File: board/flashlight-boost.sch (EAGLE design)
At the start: 9 parts

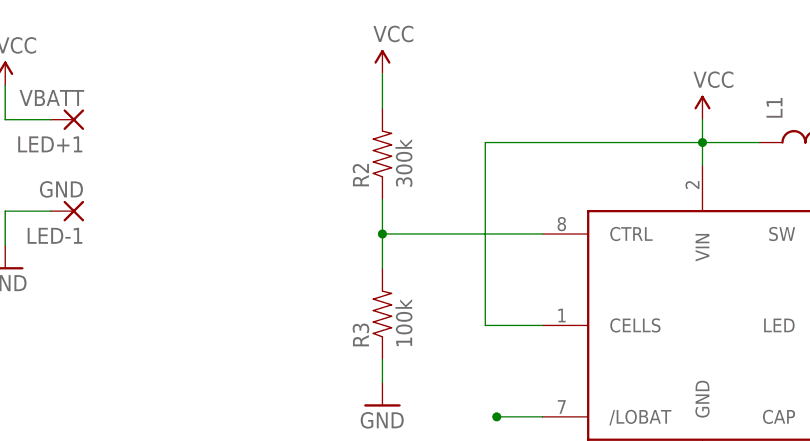
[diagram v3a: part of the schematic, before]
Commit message: Fixing voltage divider.
The voltage divider was setup to yield a control voltage of 0.6v which for a 2.4v input sets up the LED driver for a driver current of just over 25mA.  The drive current should be between 80mA and 100mA.  Lowering R1 in the divider to somewhere between 178k and 150k will do just that.
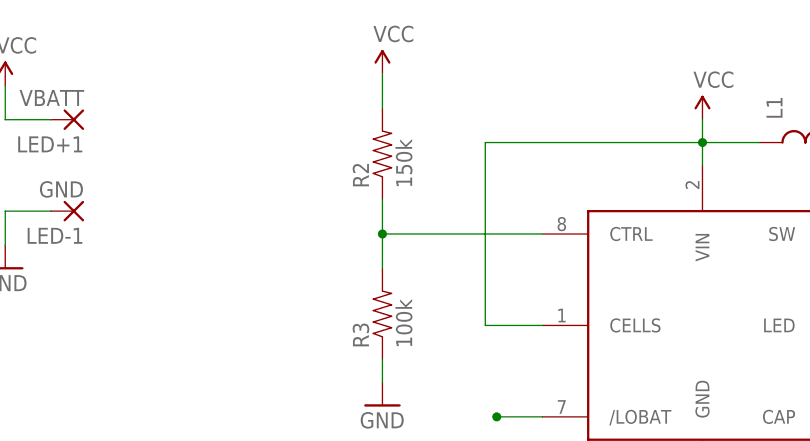
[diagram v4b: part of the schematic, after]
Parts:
- R2: value 300k -> 150k
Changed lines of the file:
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@@
 <setting verticaltext="up"/>
 </settings>
-<grid distance="0.05" unitdist="inch" unit="inch" style="lines" multiple="1" display="yes" altdistance="0.005" altunitdist="inch" altunit="inch"/>
+<grid distance="0.1" unitdist="inch" unit="inch" style="lines" multiple="1" display="no" altdistance="0.01" altunitdist="inch" altunit="inch"/>
 <layers>
-<layer number="1" name="Top" color="4" fill="1" visible="yes" active="no"/>
-<layer number="16" name="Bottom" color="1" fill="1" visible="yes" active="no"/>
-<layer number="17" name="Pads" color="2" fill="1" visible="yes" active="no"/>
-<layer number="18" name="Vias" color="2" fill="1" visible="yes" active="no"/>
-<layer number="19" name="Unrouted" color="6" fill="1" visible="yes" active="no"/>
-<layer number="20" name="Dimension" color="15" fill="1" visible="yes" active="no"/>
-<layer number="21" name="tPlace" color="16" fill="1" visible="yes" active="no"/>
-<layer number="22" name="bPlace" color="14" fill="1" visible="yes" active="no"/>
-<layer number="23" name="tOrigins" color="15" fill="1" visible="yes" active="no"/>
-<layer number="24" name="bOrigins" color="15" fill="1" visible="yes" active="no"/>
-<layer number="25" name="tNames" color="7" fill="1" visible="yes" active="no"/>
-<layer number="26" name="bNames" color="7" fill="1" visible="yes" active="no"/>
-<layer number="27" name="tValues" color="7" fill="1" visible="yes" active="no"/>
-<layer number="28" name="bValues" color="7" fill="1" visible="yes" active="no"/>
+<layer number="1" name="Top" color="4" fill="1" visible="no" active="no"/>
+<layer number="16" name="Bottom" color="1" fill="1" visible="no" active="no"/>
+<layer number="17" name="Pads" color="2" fill="1" visible="no" active="no"/>
+<layer number="18" name="Vias" color="2" fill="1" visible="no" active="no"/>
+<layer number="19" name="Unrouted" color="6" fill="1" visible="no" active="no"/>
+<layer number="20" name="Dimension" color="15" fill="1" visible="no" active="no"/>
+<layer number="21" name="tPlace" color="16" fill="1" visible="no" active="no"/>
+<layer number="22" name="bPlace" color="14" fill="1" visible="no" active="no"/>
+<layer number="23" name="tOrigins" color="15" fill="1" visible="no" active="no"/>
+<layer number="24" name="bOrigins" color="15" fill="1" visible="no" active="no"/>
+<layer number="25" name="tNames" color="7" fill="1" visible="no" active="no"/>
+<layer number="26" name="bNames" color="7" fill="1" visible="no" active="no"/>
+<layer number="27" name="tValues" color="7" fill="1" visible="no" active="no"/>
+<layer number="28" name="bValues" color="7" fill="1" visible="no" active="no"/>
 <layer number="29" name="tStop" color="7" fill="3" visible="no" active="no"/>
 <layer number="30" name="bStop" color="7" fill="6" visible="no" active="no"/>
@@
 <layer number="35" name="tGlue" color="7" fill="4" visible="no" active="no"/>
 <layer number="36" name="bGlue" color="7" fill="5" visible="no" active="no"/>
-<layer number="37" name="tTest" color="7" fill="1" visible="yes" active="no"/>
-<layer number="38" name="bTest" color="7" fill="1" visible="yes" active="no"/>
+<layer number="37" name="tTest" color="7" fill="1" visible="no" active="no"/>
+<layer number="38" name="bTest" color="7" fill="1" visible="no" active="no"/>
 <layer number="39" name="tKeepout" color="4" fill="11" visible="no" active="no"/>
 <layer number="40" name="bKeepout" color="1" fill="11" visible="no" active="no"/>
@@
 <layer number="44" name="Drills" color="7" fill="1" visible="no" active="no"/>
 <layer number="45" name="Holes" color="7" fill="1" visible="no" active="no"/>
-<layer number="46" name="Milling" color="3" fill="1" visible="yes" active="no"/>
-<layer number="47" name="Measures" color="7" fill="1" visible="yes" active="no"/>
-<layer number="48" name="Document" color="7" fill="1" visible="yes" active="no"/>
-<layer number="49" name="Reference" color="7" fill="1" visible="yes" active="no"/>
-<layer number="50" name="dxf" color="7" fill="1" visible="yes" active="no"/>
-<layer number="51" name="tDocu" color="6" fill="1" visible="yes" active="no"/>
-<layer number="52" name="bDocu" color="7" fill="1" visible="yes" active="no"/>
-<layer number="53" name="tGND_GNDA" color="7" fill="9" visible="yes" active="no"/>
-<layer number="54" name="bGND_GNDA" color="1" fill="9" visible="yes" active="no"/>
-<layer number="56" name="wert" color="7" fill="1" visible="yes" active="no"/>
+<layer number="46" name="Milling" color="3" fill="1" visible="no" active="no"/>
+<layer number="47" name="Measures" color="7" fill="1" visible="no" active="no"/>
+<layer number="48" name="Document" color="7" fill="1" visible="no" active="no"/>
+<layer number="49" name="Reference" color="7" fill="1" visible="no" active="no"/>
+<layer number="50" name="dxf" color="7" fill="1" visible="no" active="no"/>
+<layer number="51" name="tDocu" color="6" fill="1" visible="no" active="no"/>
+<layer number="52" name="bDocu" color="7" fill="1" visible="no" active="no"/>
+<layer number="53" name="tGND_GNDA" color="7" fill="9" visible="no" active="no"/>
+<layer number="54" name="bGND_GNDA" color="1" fill="9" visible="no" active="no"/>
+<layer number="56" name="wert" color="7" fill="1" visible="no" active="no"/>
 <layer number="91" name="Nets" color="2" fill="1" visible="yes" active="yes"/>
 <layer number="92" name="Busses" color="1" fill="1" visible="yes" active="yes"/>
@@
 <part name="GND1" library="SparkFun-Aesthetics" deviceset="GND" device=""/>
 <part name="SUPPLY2" library="SparkFun-Aesthetics" deviceset="VCC" device=""/>
-<part name="R2" library="SparkFun-Resistors" deviceset="RESISTOR" device="0603-RES" value="300k"/>
+<part name="R2" library="SparkFun-Resistors" deviceset="RESISTOR" device="0603-RES" value="150k"/>
 <part name="R3" library="SparkFun-Resistors" deviceset="RESISTOR" device="0603-RES" value="100k"/>
 <part name="SUPPLY3" library="SparkFun-Aesthetics" deviceset="VCC" device=""/>
